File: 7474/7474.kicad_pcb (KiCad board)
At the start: 2 copper layers, 64 x 65.5 mm, 49 parts, among them J1 USB, J10 Conn_02x03_Odd_Even, J11 Conn_02x03_Odd_Even, J12 Conn_02x03_Odd_Even, J13 Conn_02x03_Odd_Even, J14 Conn_02x03_Odd_Even, J15 Conn_02x03_Odd_Even, J16 Conn_02x03_Odd_Even, J17 Conn_02x03_Odd_Even, J18 Conn_02x03_Odd_Even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

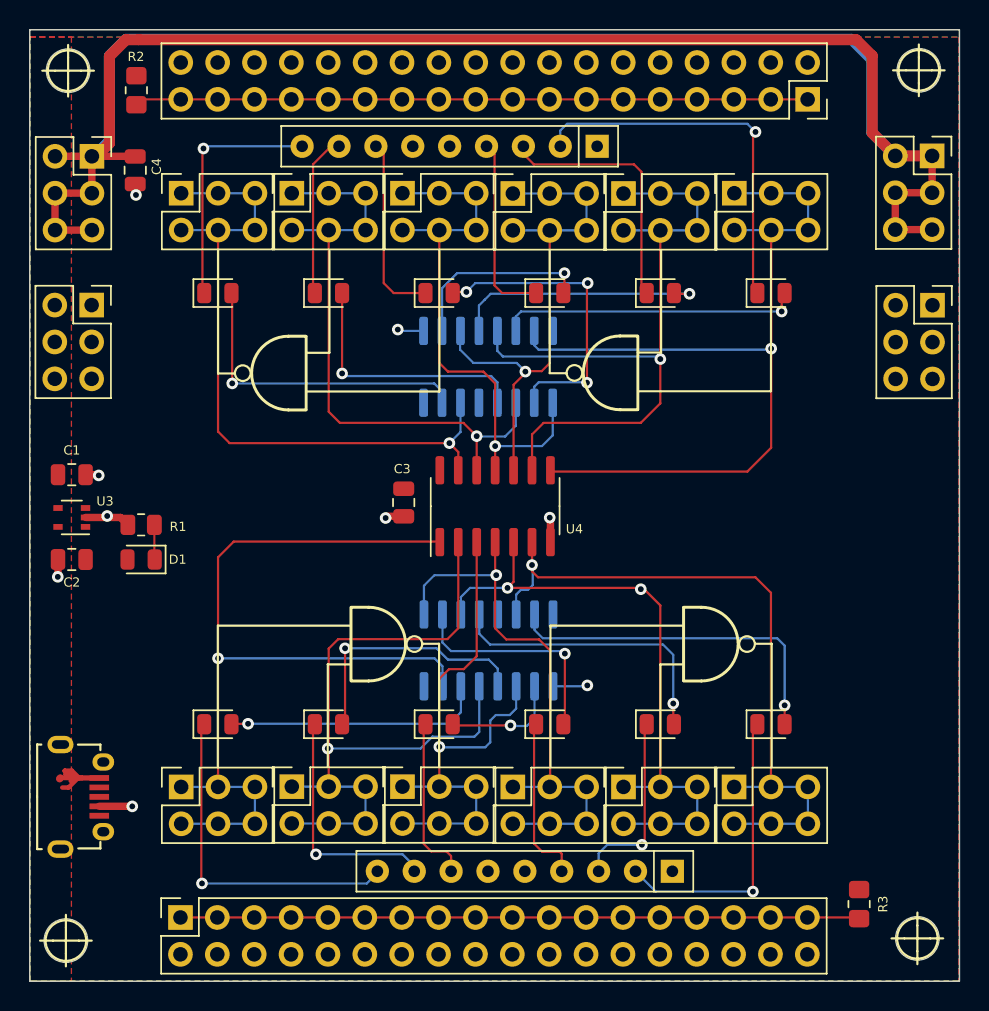
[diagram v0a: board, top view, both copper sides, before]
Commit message: Simplificação do circuito. Inclusão da placa 7474.
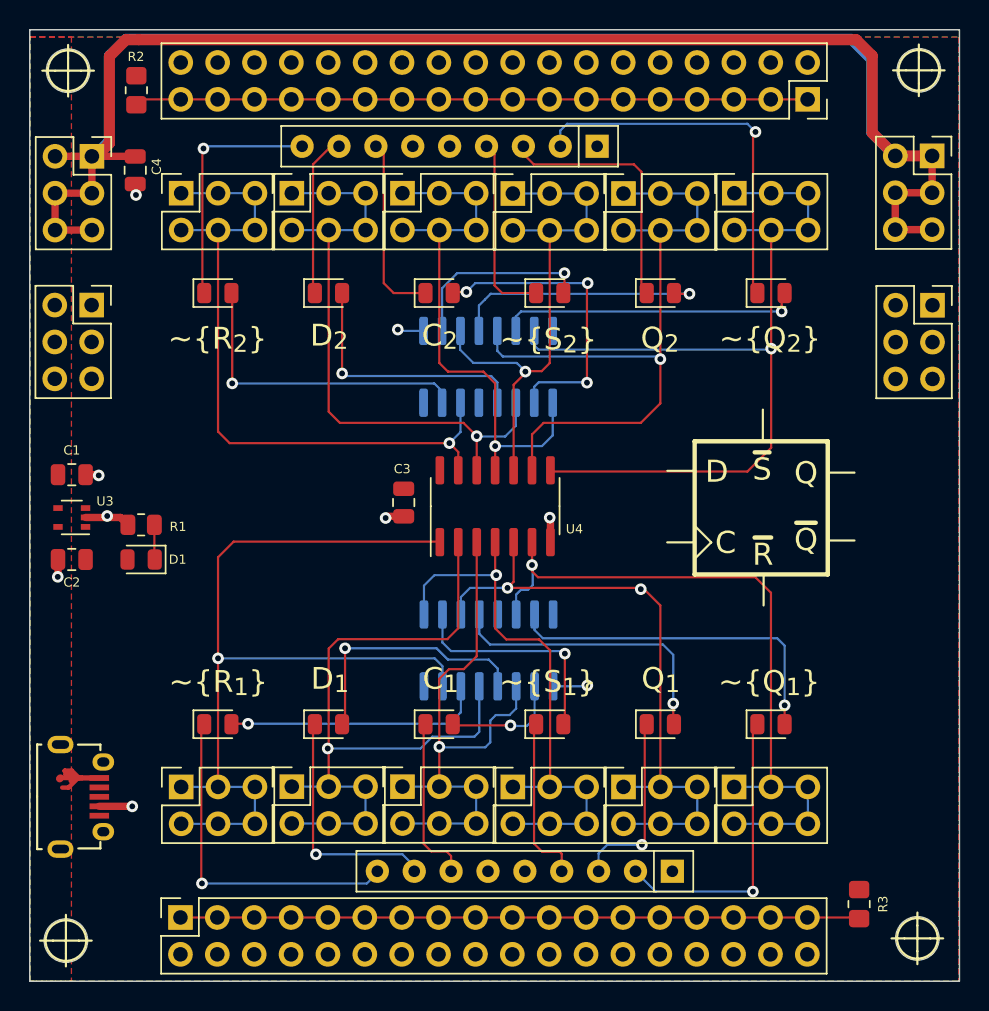
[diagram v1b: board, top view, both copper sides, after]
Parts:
- U4: value 7400 -> 7474
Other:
- board text added: "C"
- board text added: "C_{1}"
- board text added: "C_{2}"
- board text added: "D"
- board text added: "D_{1}"
- board text added: "D_{2}"
- board text added: "Q"
- board text added: "Q_{1}"
- board text added: "Q_{2}"
- board text added: "~{Q_{1}}"
- board text added: "~{Q_{2}}"
- board text added: "~{Q}"
- board text added: "~{R_{1}}"
- board text added: "~{R_{2}}"
- board text added: "~{R}"
- board text added: "~{S_{1}}"
- board text added: "~{S_{2}}"
- board text added: "~{S}"
